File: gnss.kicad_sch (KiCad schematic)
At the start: 26 parts, among them J401 GNSS ANT pads, U401 AT6558R-5N32, X401 TCXO 26MHz, X402 32.768kHz

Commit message: Update schematic wiring
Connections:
- net GNSS_ANT_FEED: no longer C402.1, J401.1 (In), L401.1
- new net: C402.1, J401.1 (In), L401.1
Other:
- moved on the sheet: C404, C405, C407, C411, J401

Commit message: Adjust layout and schematic
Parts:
- removed C414: 100m, cc1200_balloon:SuperCap_KEMET_FCS_D10.7mm, symbol Device:C_Polarized
- J401: value GNSS ANT pads -> GNSS ANT
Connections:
- net GNSS_ANT: now reaches C402.1, J401.1 (In), L401.1
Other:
- moved on the sheet: C401, C402, C403, C404, C405, C406, C407, C408, C409, C410, C411, C412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

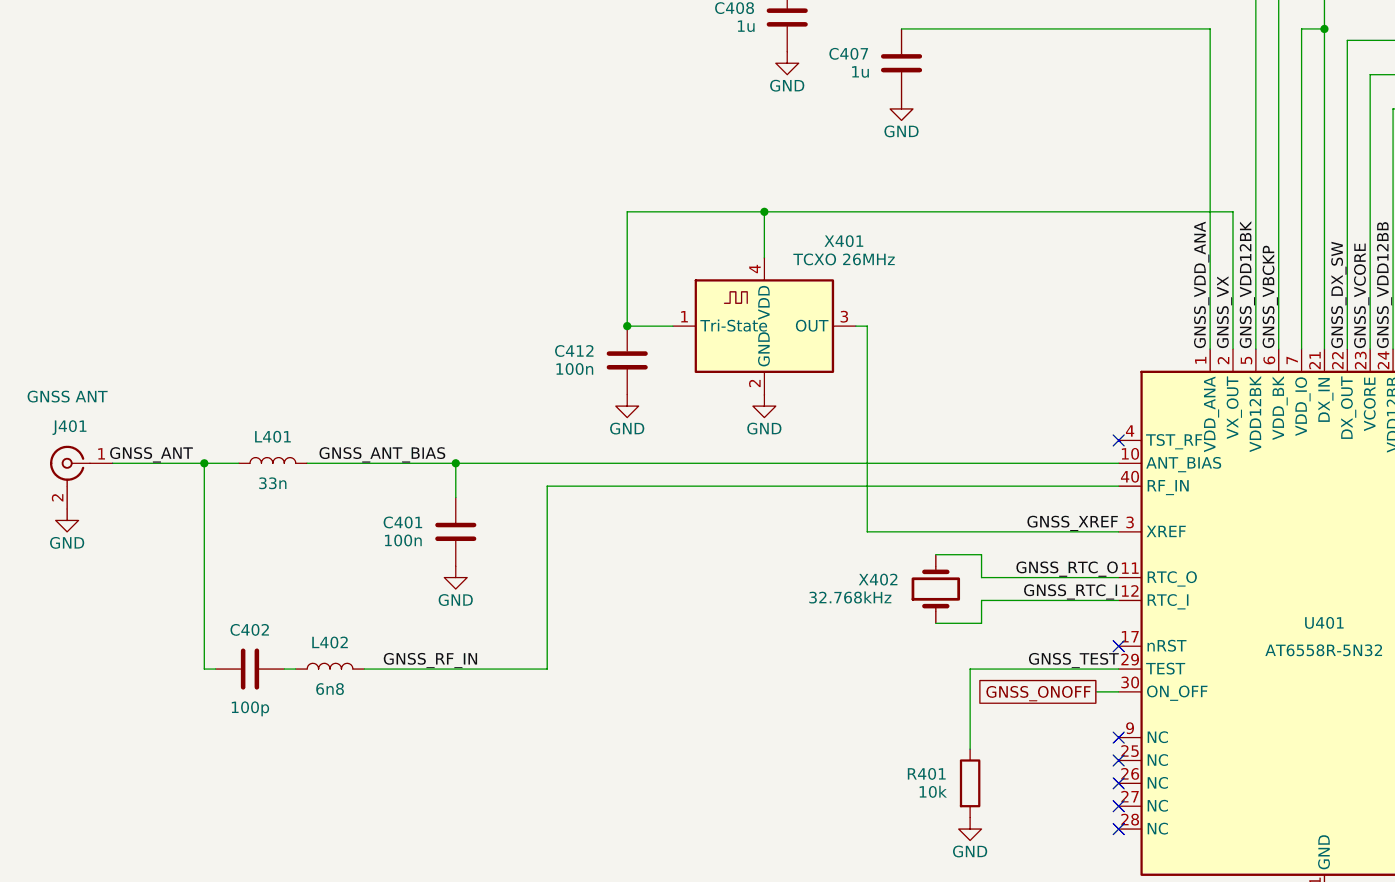
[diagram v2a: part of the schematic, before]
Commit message: Clean up schematic. Add component groups to PCB.
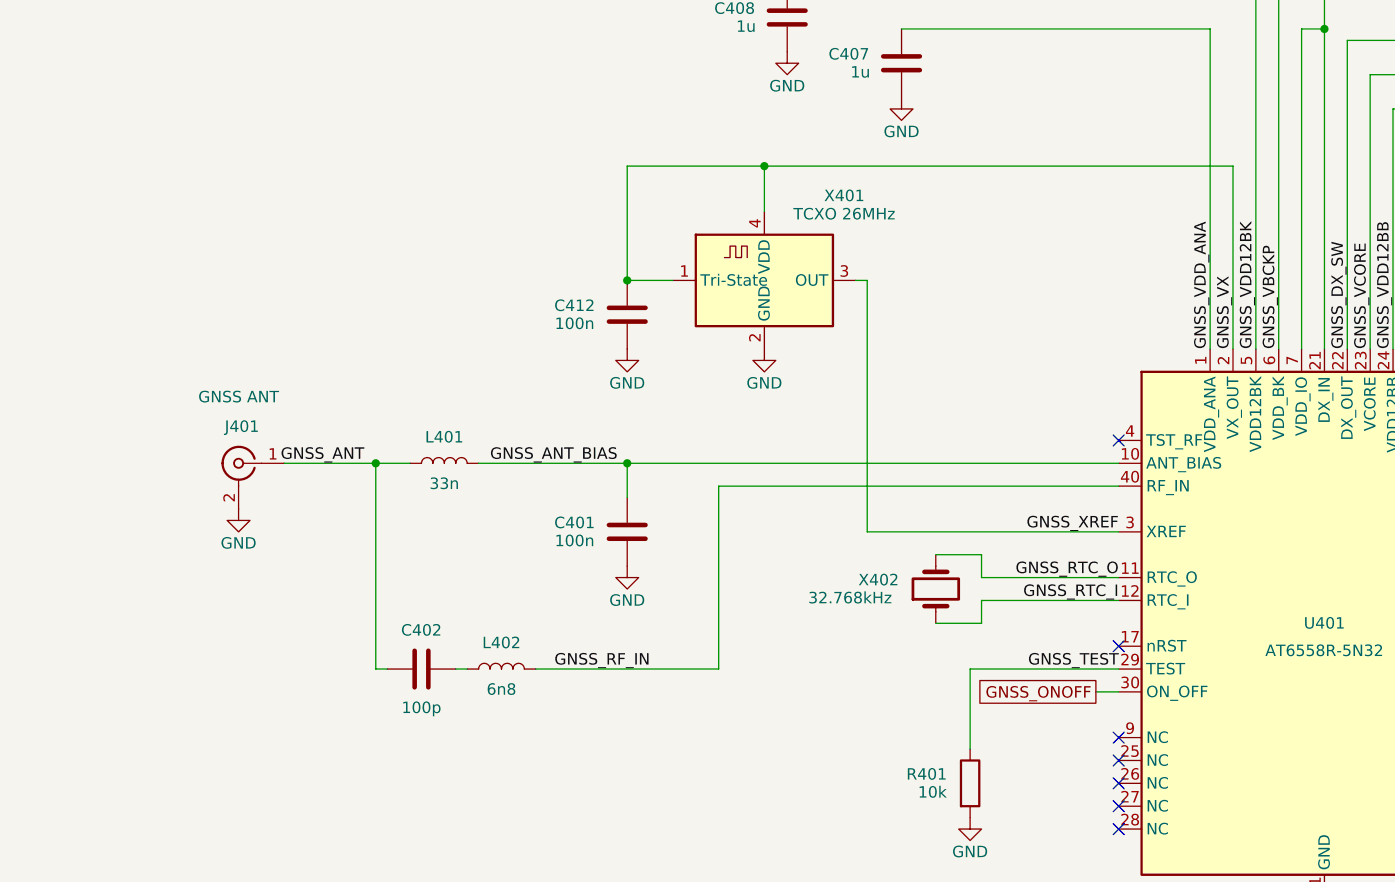
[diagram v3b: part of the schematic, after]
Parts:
- J401: footprint cc1200_balloon:SolderPad_Coax_Pigtail -> Connector_Coaxial:SMA_Samtec_SMA-J-P-H-ST-EM1_EdgeMount
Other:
- moved on the sheet: C401, C402, C412, J401, L401, L402, X401

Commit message: Inital routing
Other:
- moved on the sheet: C407, C408
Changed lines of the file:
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@@
 	(wire
 		(pts
-			(xy 146.05 41.91) (xy 198.12 41.91)
+			(xy 173.99 41.91) (xy 198.12 41.91)
 		)
 		(stroke
@@
 	(wire
 		(pts
-			(xy 158.75 46.99) (xy 193.04 46.99)
+			(xy 185.42 46.99) (xy 193.04 46.99)
 		)
 		(stroke
@@
 	(symbol
 		(lib_id "power:GND")
-		(at 146.05 49.53 0)
+		(at 173.99 49.53 0)
 		(unit 1)
 		(body_style 1)
@@
 		(dnp no)
 		(property "Reference" "#PWR4014"
-			(at 146.05 55.88 0)
+			(at 173.99 55.88 0)
 			(hide yes)
 			(show_name no)
@@
 		)
 		(property "Value" "GND"
-			(at 146.05 53.34 0)
+			(at 173.99 53.34 0)
 			(show_name no)
 			(do_not_autoplace no)
@@
 		)
 		(property "Footprint" ""
-			(at 146.05 49.53 0)
+			(at 173.99 49.53 0)
 			(hide yes)
 			(show_name no)
@@
 		)
 		(property "Datasheet" ""
-			(at 146.05 49.53 0)
+			(at 173.99 49.53 0)
 			(hide yes)
 			(show_name no)
@@
 		)
 		(property "Description" ""
-			(at 146.05 49.53 0)
+			(at 173.99 49.53 0)
 			(hide yes)
 			(show_name no)
@@
 	(symbol
 		(lib_id "Device:C")
-		(at 146.05 45.72 0)
+		(at 173.99 45.72 0)
 		(unit 1)
 		(body_style 1)
@@
 		(dnp no)
 		(property "Reference" "C408"
-			(at 140.208 44.72 0)
+			(at 168.148 44.72 0)
 			(show_name no)
 			(do_not_autoplace no)
@@
 		)
 		(property "Value" "1u"
-			(at 141.478 46.72 0)
+			(at 169.418 46.72 0)
 			(show_name no)
 			(do_not_autoplace no)
@@
 		)
 		(property "Footprint" "Capacitor_SMD:C_0402_1005Metric"
-			(at 146.05 45.72 0)
+			(at 173.99 45.72 0)
 			(hide yes)
 			(show_name no)
@@
 		)
 		(property "Datasheet" ""
-			(at 146.05 45.72 0)
+			(at 173.99 45.72 0)
 			(hide yes)
 			(show_name no)
@@
 		)
 		(property "Description" ""
-			(at 146.05 45.72 0)
+			(at 173.99 45.72 0)
 			(hide yes)
 			(show_name no)
@@
 	(symbol
 		(lib_id "Device:C")
-		(at 158.75 50.8 0)
+		(at 185.42 50.8 0)
 		(unit 1)
 		(body_style 1)
@@
 		(dnp no)
 		(property "Reference" "C407"
-			(at 152.908 49.8 0)
+			(at 179.578 49.8 0)
 			(show_name no)
 			(do_not_autoplace no)
@@
 		)
 		(property "Value" "1u"
-			(at 154.178 51.8 0)
+			(at 180.848 51.8 0)
 			(show_name no)
 			(do_not_autoplace no)
@@
 		)
 		(property "Footprint" "Capacitor_SMD:C_0402_1005Metric"
-			(at 158.75 50.8 0)
+			(at 185.42 50.8 0)
 			(hide yes)
 			(show_name no)
@@
 		)
 		(property "Datasheet" ""
-			(at 158.75 50.8 0)
+			(at 185.42 50.8 0)
 			(hide yes)
 			(show_name no)
@@
 		)
 		(property "Description" ""
-			(at 158.75 50.8 0)
+			(at 185.42 50.8 0)
 			(hide yes)
 			(show_name no)
@@
 	(symbol
 		(lib_id "power:GND")
-		(at 158.75 54.61 0)
+		(at 185.42 54.61 0)
 		(unit 1)
 		(body_style 1)
@@
 		(dnp no)
 		(property "Reference" "#PWR4013"
-			(at 158.75 60.96 0)
+			(at 185.42 60.96 0)
 			(hide yes)
 			(show_name no)
@@
 		)
 		(property "Value" "GND"
-			(at 158.75 58.42 0)
+			(at 185.42 58.42 0)
 			(show_name no)
 			(do_not_autoplace no)
@@
 		)
 		(property "Footprint" ""
-			(at 158.75 54.61 0)
+			(at 185.42 54.61 0)
 			(hide yes)
 			(show_name no)
@@
 		)
 		(property "Datasheet" ""
-			(at 158.75 54.61 0)
+			(at 185.42 54.61 0)
 			(hide yes)
 			(show_name no)
@@
 		)
 		(property "Description" ""
-			(at 158.75 54.61 0)
+			(at 185.42 54.61 0)
 			(hide yes)
 			(show_name no)
